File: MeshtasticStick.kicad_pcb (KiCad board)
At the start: 2 copper layers, 31 x 60 mm, 3 parts

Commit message: ver1
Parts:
- removed REF**: ESP32-PICO-MINI-02, PCM_Espressif:ESP32-PICO-MINI-02
- removed REF**: E22-900M22S, RF_Module:E22-900M22S
- removed REF**: TestPoint_Bridge_Pitch2.0mm_Drill0.7mm, TestPoint:TestPoint_Bridge_Pitch2.0mm_Drill0.7mm
- added BT1: Battery_Cell, Connector_PinHeader_2.54mm:PinHeader_1x02_P2.54mm_Vertical, F.Cu at (126.5, 146.8)
- added C1: 1uF, Capacitor_SMD:C_0603_1608Metric, F.Cu at (149.8, 112.9)
- added C10: 14p, Capacitor_SMD:C_0603_1608Metric, F.Cu at (144.1, 128.3)
- added C11: 1nF, Capacitor_SMD:C_0201_0603Metric, F.Cu at (150.0, 159.5)
- added C12: 47uF, Capacitor_SMD:CP_Elec_6.3x7.7, F.Cu at (143.3, 147.5)
- added C13: 10nF, Capacitor_SMD:C_0603_1608Metric, F.Cu at (138.2, 140.9)
- added C14: 4.7uF, Capacitor_SMD:C_0603_1608Metric, F.Cu at (129.8, 146.0)
- added C15: 1nF, Capacitor_SMD:C_0603_1608Metric, F.Cu at (129.8, 143.5)
- added C16: 0.1uF, Capacitor_SMD:C_0603_1608Metric, F.Cu at (151.9, 132.3)
- added C17: 10uF, Capacitor_SMD:C_0603_1608Metric, F.Cu at (146.3, 136.7)
- added C18: 0.1uF, Capacitor_SMD:C_0603_1608Metric, F.Cu at (146.3, 135.1)
- added C19: 22uF, Capacitor_SMD:C_0603_1608Metric, F.Cu at (154.7, 132.8)
- added C2: 1uF, Capacitor_SMD:C_0603_1608Metric, F.Cu at (149.8, 110.4)
- added C20: 22uF, Capacitor_SMD:C_0603_1608Metric, F.Cu at (154.7, 131.1)
- added C21: 22nF, Capacitor_SMD:C_0603_1608Metric, F.Cu at (148.4, 128.5)
- added C3: 1uF, Capacitor_SMD:C_0201_0603Metric, F.Cu at (150.0, 154.2)
- added C4: 4.7uF, Capacitor_SMD:C_0603_1608Metric, F.Cu at (129.7, 117.5)
- added C5: 4.7uF, Capacitor_SMD:C_0603_1608Metric, F.Cu at (142.1, 123.8)
- added C6: 1nF, Capacitor_SMD:C_0201_0603Metric, F.Cu at (150.0, 156.0)
- added C7: 100uF, Capacitor_SMD:CP_Elec_6.3x7.7, F.Cu at (134.6, 112.9)
- added C8: 10uF, Capacitor_SMD:C_0201_0603Metric, F.Cu at (150.0, 157.7)
- added C9: 14p, Capacitor_SMD:C_0603_1608Metric, F.Cu at (144.1, 126.4)
- added D1: MBR120VLSFT1G, Diode_SMD:D_SOD-123F, F.Cu at (141.7, 116.2)
- added D2: SMM4F5.0A, Diode_SMD:D_SMP_DO-220AA, F.Cu at (127.1, 156.8)
- added D3: MBR120VLSFT1G, Diode_SMD:D_SOD-123F, F.Cu at (154.5, 127.5)
- added F1: Fuse, Fuse:Fuse_1210_3225Metric, F.Cu at (141.0, 111.1)
- added J1: TYPE-C-31-M-12, TYPE-C-31-M-12 footprint:HRO_TYPE-C-31-M-12, F.Cu at (154.3, 119.7)
- added J2: Conn_02x05_Odd_Even, Connector_PinHeader_1.27mm:PinHeader_2x05_P1.27mm_Vertical, F.Cu at (127.0, 109.9)
- added J3: Conn_01x04, Connector_PinHeader_2.54mm:PinHeader_1x04_P2.54mm_Vertical, F.Cu at (129.5, 132.7)
- added J4: Conn_01x04, Connector_PinHeader_2.54mm:PinHeader_1x04_P2.54mm_Vertical, F.Cu at (129.6, 135.9)
- added J5: Conn_01x02, Connector_PinHeader_2.54mm:PinHeader_1x02_P2.54mm_Vertical, F.Cu at (132.6, 160.8)
- added JP1: SolderJumper_3_Bridged12, Jumper:SolderJumper-3_P1.3mm_Open_RoundedPad1.0x1.5mm, B.Cu at (126.4, 134.7)
- added JP2: Jumper_2_Bridged, Jumper:SolderJumper-2_P1.3mm_Bridged2Bar_RoundedPad1.0x1.5mm, F.Cu at (135.6, 141.1)
- added JP3: Jumper_2_Bridged, Jumper:SolderJumper-2_P1.3mm_Bridged2Bar_RoundedPad1.0x1.5mm, F.Cu at (133.1, 141.1)
- added JP4: Jumper_2_Open, Jumper:SolderJumper-2_P1.3mm_Open_RoundedPad1.0x1.5mm, F.Cu at (134.1, 150.6)
- added L1: 10uH, Inductor_SMD:L_1210_3225Metric, F.Cu at (142.2, 120.0)
- added L2: 10uH, Fuse:Fuse_1210_3225Metric, F.Cu at (142.9, 155.2)
- added L3: MDA4020-1R0M 6.8uH/8.5A/16mR, Inductor_SMD:L_Coilcraft_XAL6060-XXX, F.Cu at (151.6, 137.9)
- added R1: 10K, Capacitor_SMD:C_0603_1608Metric, F.Cu at (145.5, 109.1)
- added R10: 2.2M, Capacitor_SMD:C_0603_1608Metric, F.Cu at (153.1, 156.4)
- added R11: 820K, Capacitor_SMD:C_0603_1608Metric, F.Cu at (153.1, 158.9)
- added R12: 27R, Capacitor_SMD:C_0603_1608Metric, F.Cu at (146.5, 119.4)
- added R13: 27R, Capacitor_SMD:C_0603_1608Metric, F.Cu at (146.5, 117.5)
- added R14: 3.3K, Capacitor_SMD:C_0603_1608Metric, F.Cu at (130.0, 147.5)
- added R15: 1K, Capacitor_SMD:C_0603_1608Metric, F.Cu at (129.8, 142.0)
- added R16: 24K, Capacitor_SMD:C_0603_1608Metric, F.Cu at (138.7, 150.6)
- added R17: DNM, Capacitor_SMD:C_0603_1608Metric, F.Cu at (130.0, 150.8)
- added R18: DNM, Capacitor_SMD:C_0603_1608Metric, F.Cu at (136.7, 150.6)
- added R19: 470R, Capacitor_SMD:C_0603_1608Metric, F.Cu at (129.9, 140.1)
- added R2: 5.1K, Capacitor_SMD:C_0603_1608Metric, F.Cu at (146.5, 121.3)
- added R20: DNM, Capacitor_SMD:C_0603_1608Metric, F.Cu at (135.4, 153.1)
- added R21: DNM, Capacitor_SMD:C_0603_1608Metric, F.Cu at (131.6, 150.9)
- added R22: 90.9K, Capacitor_SMD:C_0603_1608Metric, F.Cu at (146.6, 131.8)
- added R23: 68K, Capacitor_SMD:C_0603_1608Metric, F.Cu at (151.9, 128.5)
- added R24: 10K, Capacitor_SMD:C_0603_1608Metric, F.Cu at (146.6, 128.5)
- added R25: 18K, Capacitor_SMD:C_0603_1608Metric, F.Cu at (150.1, 128.5)
- added R26: 100K, Capacitor_SMD:C_0603_1608Metric, F.Cu at (144.0, 135.9)
- added R27: 10K, Capacitor_SMD:C_0603_1608Metric, F.Cu at (147.4, 126.2)
- added R3: 5.1K, Capacitor_SMD:C_0603_1608Metric, F.Cu at (146.7, 115.6)
- added R4: 1K, Capacitor_SMD:C_0603_1608Metric, F.Cu at (141.5, 159.5)
- added R5: 1K, Capacitor_SMD:C_0603_1608Metric, F.Cu at (144.0, 159.5)
- added R6: 1K, Capacitor_SMD:C_0603_1608Metric, F.Cu at (153.1, 146.4)
- added R7: DNM, Capacitor_SMD:C_0603_1608Metric, F.Cu at (153.1, 148.9)
- added R8: 0R, Capacitor_SMD:C_0603_1608Metric, F.Cu at (153.1, 151.4)
- added R9: 0R, Capacitor_SMD:C_0603_1608Metric, F.Cu at (153.1, 153.9)
- added U1: AP2112K-3.3, Package_TO_SOT_SMD:SOT-23-5, F.Cu at (145.2, 112.6)
- added U2: SPV1040T, STMicroelectronics SPV1040T:SOP65P640X120-8N, F.Cu at (133.6, 156.7)
- added U3: E22-900M30S, E22-900M30S footprint:XCVR_E22-900M30S, F.Cu at (140.8, 88.3)
- added U4: MDBT50Q-P1MV2, RF_Module:Raytac_MDBT50Q, F.Cu at (132.1, 124.5)
- added U5: L6924D, L6924D footprint:QFN50P300X300X100-17N, F.Cu at (134.7, 146.1)
- added U6: MP2338GTL, Package_TO_SOT_SMD:SOT-583-8, F.Cu at (149.4, 132.3)
- added Y1: Crystal, Crystal:Crystal_SMD_2012-2Pin_2.0x1.2mm, F.Cu at (141.6, 127.7)
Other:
- board size 31 x 60 mm -> 31.1 x 94.2 mm

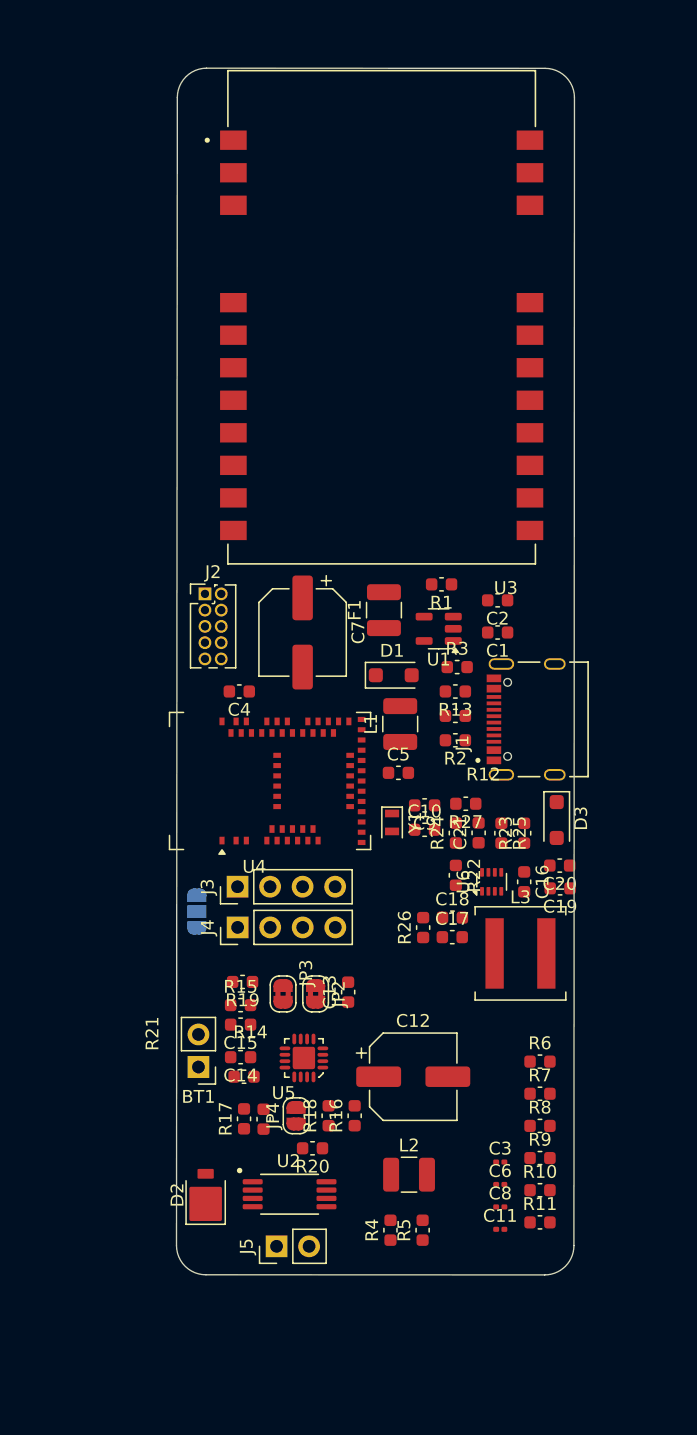
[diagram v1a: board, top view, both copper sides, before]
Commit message: [fix] Fix power supply issue and capacitor packaging, complete initial routing
- Fixed power supply issue to improve stability
- Adjusted certain capacitor packages to meet design requirements
- Completed initial PCB routing
- Corrected OLED signal routing to ensure proper display
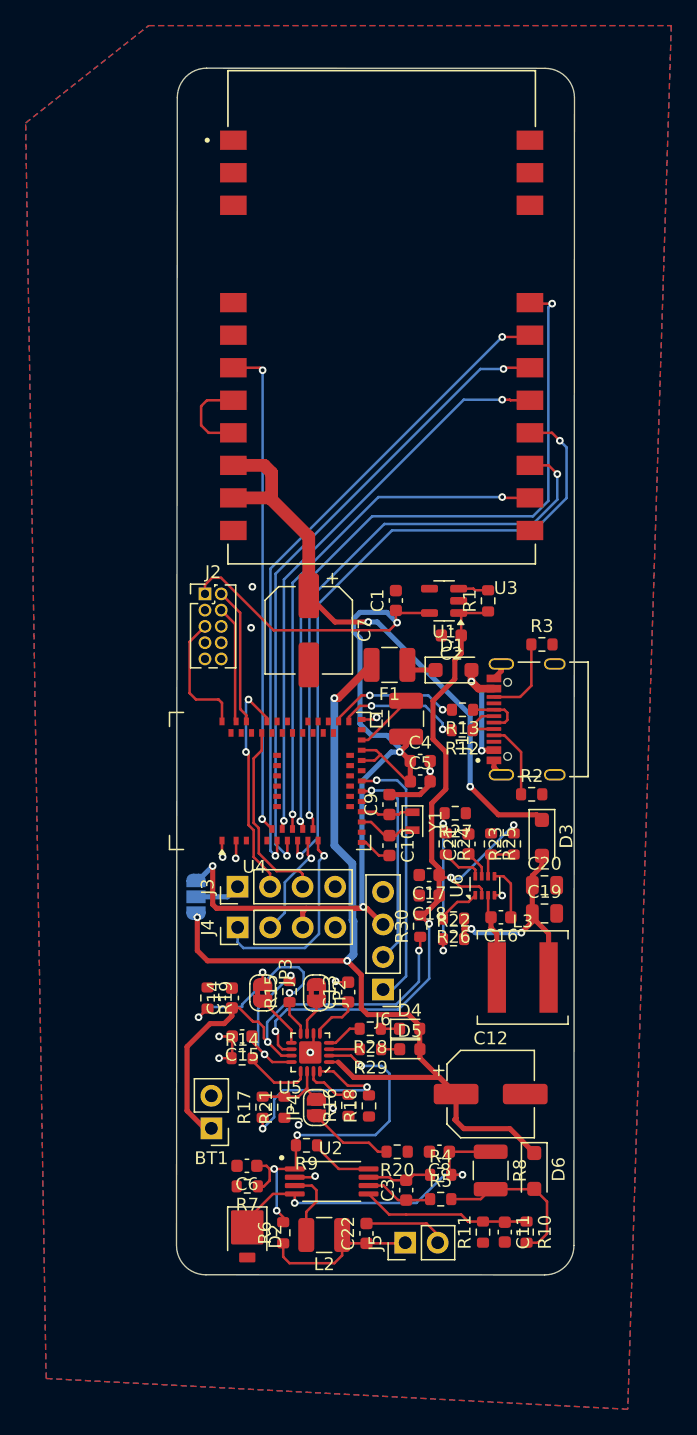
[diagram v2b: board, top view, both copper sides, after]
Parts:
- added C22: 10uF, Capacitor_SMD:C_0603_1608Metric, F.Cu at (139.6, 159.8)
- added D4: LED, LED_SMD:LED_0603_1608Metric, F.Cu at (143.0, 143.8)
- added D5: LED, LED_SMD:LED_0603_1608Metric, F.Cu at (143.0, 145.4)
- added D6: MBR120VLSFT1G, Diode_SMD:D_SOD-123F, F.Cu at (152.7, 154.9)
- added J6: Conn_01x04, Connector_PinHeader_2.54mm:PinHeader_1x04_P2.54mm_Vertical, F.Cu at (140.9, 140.7)
- added R28: 1K, Resistor_SMD:R_0603_1608Metric, F.Cu at (139.9, 143.8)
- added R29: 1K, Resistor_SMD:R_0603_1608Metric, F.Cu at (139.9, 145.4)
- added R30: 0R, Resistor_SMD:R_0603_1608Metric, F.Cu at (143.8, 135.8)
- C11, C3, C8: footprint Capacitor_SMD:C_0201_0603Metric -> Capacitor_SMD:C_0603_1608Metric
- C19, C20: footprint Capacitor_SMD:C_0603_1608Metric -> Capacitor_SMD:C_0805_2012Metric
- C6: value 1nF -> 100nF; footprint Capacitor_SMD:C_0201_0603Metric -> Capacitor_SMD:C_0603_1608Metric
- R1, R10, R11, R12, R13, R14, R15, R16, R17, R18, R19, R2, R20, R21, R22, R23, R24, R25, R26, R27, R3, R4, R5, R6, R7, R9: footprint Capacitor_SMD:C_0603_1608Metric -> Resistor_SMD:R_0603_1608Metric
- R8: value 0R -> 10mR; footprint Capacitor_SMD:C_0603_1608Metric -> Resistor_SMD:R_1210_3225Metric
- moved R6 24.1 mm to (133.1, 159.7), turned to 90 degrees
- moved R7 24.0 mm to (130.3, 156.1), turned to 180 degrees
- moved C6 19.8 mm to (130.3, 154.5), turned to 180 degrees
- moved R9 18.3 mm to (134.9, 152.9), turned to 180 degrees
- moved C4 15.1 mm to (143.8, 122.9), turned to 0 degrees
- moved J5 10.0 mm to (142.6, 160.5)
- moved C1 8.33 mm to (141.9, 110.4), turned to 90 degrees
- moved L2 8.13 mm to (136.3, 159.9), turned to 180 degrees
- moved C3 7.66 mm to (142.7, 156.4), turned to 90 degrees
- moved R2 7.30 mm to (152.5, 125.5), turned to 0 degrees
- moved R3 6.85 mm to (153.3, 113.8)
- moved R20 6.61 mm to (142.0, 153.4)
- moved C8 6.41 mm to (145.3, 153.4), turned to 180 degrees
- moved C12 6.19 mm to (149.3, 148.9)
- moved R4 5.84 mm to (145.4, 155.2), turned to 0 degrees
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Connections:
- BT1 pad 1: VBAT -> Net-(BT1-+)
- C12 pad 1: VOUT_SPV1040 -> 5V_USB
- C14 pad 1: VBAT -> Net-(BT1-+)
- C17 pad 1: SYS_VIN -> VBAT
- C18 pad 1: SYS_VIN -> VBAT
- C2 pad 1: 5V_USB -> VBAT
- J2 pad 1: VTref -> 3V3
- J4 pad 3: VCC -> 3V3
- R1 pad 1: 5V_USB -> VBAT
- R10 pad 2: VOUT_SPV1040 -> Vrs-
- R23 pad 2: SYS_VIN -> VBAT
- R5 pad 2: VOUT_SPV1040 -> Vrs-
- R8 pad 2: VOUT_SPV1040 -> Vrs-
- U1 pad 1: 5V_USB -> VBAT
- U4 pad 12: unconnected-(U4-P0.31-Pad12) -> OLED_SCL
- U4 pad 14: unconnected-(U4-P0.30-Pad14) -> OLED_SDA
- U4 pad 22: unconnected-(U4-P0.06-Pad22) -> DEBUG_TX
- U4 pad 24: unconnected-(U4-P0.08-Pad24) -> DEBUG_RX
- U5 pad 1: VOUT_SPV1040 -> 5V_USB
- U5 pad 11: VBAT -> Net-(BT1-+)
- U5 pad 17: unconnected-(U5-EP-Pad17) -> GND
- U5 pad 3: unconnected-(U5-ST2-Pad3) -> Net-(U5-ST2)
- U5 pad 4: unconnected-(U5-ST1-Pad4) -> Net-(U5-ST1)
- U6 pad 2: SYS_VIN -> VBAT
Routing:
- net 3V3: track 0.00 -> 84.2 mm, vias 0 -> 4
- net 5V_USB: track 0.00 -> 76.3 mm, vias 0 -> 3
- net VBAT: track 0.00 -> 62.2 mm, vias 0 -> 4
- net LORA_CS: track 0.00 -> 58.3 mm, vias 0 -> 2
- net LORA_SCK: track 0.00 -> 51.6 mm, vias 0 -> 2
- net LORA_RESET: track 0.00 -> 51.6 mm, vias 0 -> 2
- net LORA_MOSI: track 0.00 -> 50.1 mm, vias 0 -> 2
- net 5V_OUTPUT: track 0.00 -> 45.7 mm, vias 0 -> 2
- net LORA_DIO2: track 0.00 -> 45.0 mm, vias 0 -> 2
- net LORA_MISO: track 0.00 -> 44.6 mm, vias 0 -> 2
- net LORA_DIO1: track 0.00 -> 40.5 mm, vias 0 -> 2
- net SX126X_RXEN: track 0.00 -> 38.5 mm, vias 0 -> 2
- net Net-(BT1-+): track 0.00 -> 37.5 mm, vias 0 -> 2
- net GND: track 0.00 -> 34.1 mm, vias 0 -> 15
- net VIN_sns: track 0.00 -> 28.9 mm, vias 0 -> 4
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- added copper zone on B.Cu, net GND
- added copper zone on F.Cu, net GND
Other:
- board text added: "${REFERENCE}"

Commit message: [fix] Fix power supply issue and capacitor packaging, complete initial routing
- Fixed power supply issue to improve stability
- Adjusted certain capacitor packages to meet design requirements
- Completed initial PCB routing
- Corrected OLED signal routing to ensure proper display
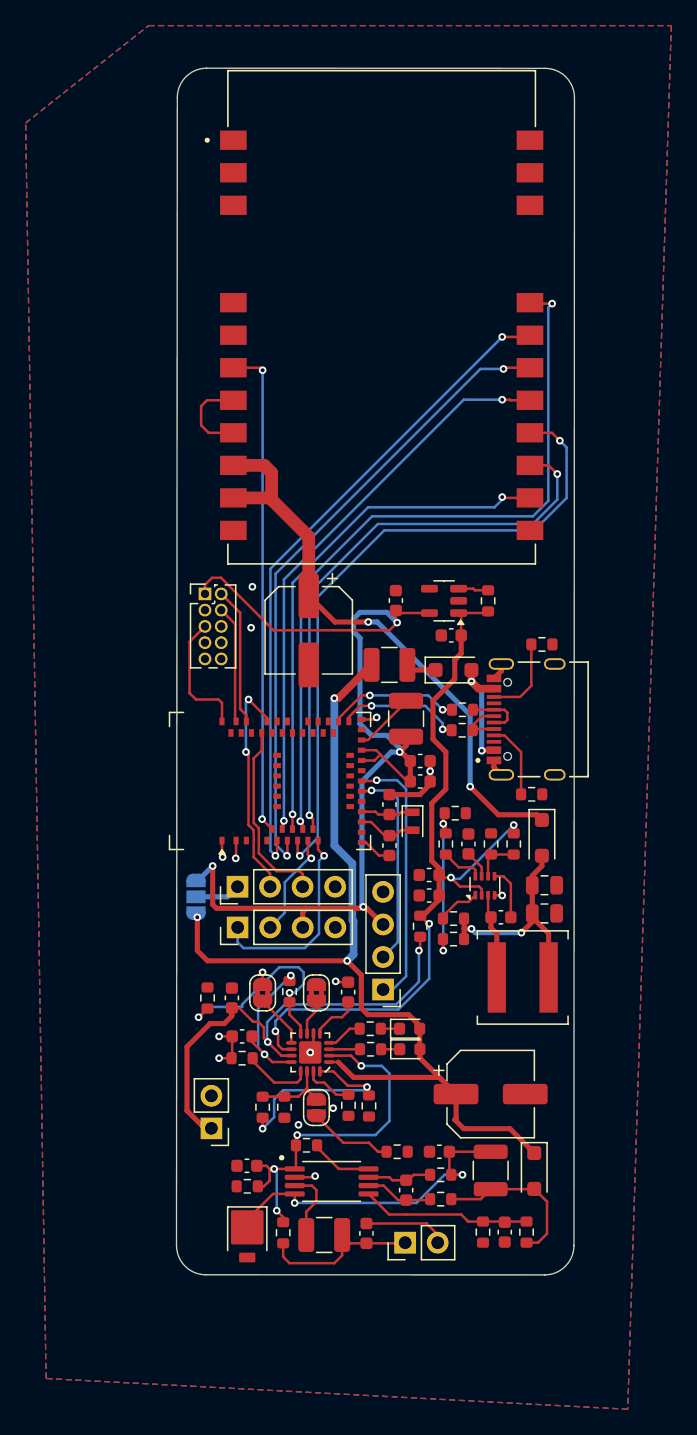
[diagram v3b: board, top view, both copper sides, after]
